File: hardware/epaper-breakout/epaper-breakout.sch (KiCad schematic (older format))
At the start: 88 parts, among them J1 XF2M-3315-1A, J2 C10418, J3 Conn_02x06_Counter_Clockwise, J4 ED060SC4, Q1 AO3401A, Q2 AO3401A, Q3 MMBT3904, Q4 MMBT3904, Q5 AO3401A, Q6 MMBT3904, U1 MCP1700-3302E_SOT23, U10 ED060SC7, U11 TP4056, U12 FS312F-G, U13 FS8205A, U2 LT1945, U3 LT1945, U4 CH340G, U5 ESP32-WROVER, U6 ED060XC5, U7 LM358, U8 74HC4094-normal, U9 MCP9700AT-ETT, Y1 Crystal_GND2

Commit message: remove battery protection, simplify
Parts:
- removed C13, C14: 10pF, Capacitor_SMD:C_0603_1608Metric, symbol Device:C
- removed C23: 0.1uF, Capacitor_SMD:C_0603_1608Metric, symbol Device:C
- removed R21: 100, Resistor_SMD:R_0805_2012Metric, symbol Device:R
- removed R22: 1k, Resistor_SMD:R_0805_2012Metric, symbol Device:R
- removed U12: FS312F-G, Package_TO_SOT_SMD:SOT-23-6, symbol epd_breakout:FS312F-G
- removed U13: FS8205A, Package_SO:TSSOP-8_4.4x3mm_P0.65mm, symbol fs8205a:FS8205A
- removed U4: CH340G, Package_SO:SOIC-16_3.9x9.9mm_P1.27mm, symbol Interface_USB:CH340G
- removed Y1: Crystal_GND2, Crystal:Crystal_SMD_3225-4Pin_3.2x2.5mm_HandSoldering, symbol Device:Crystal_GND2
- added U12: CH340C, Package_SO:SOIC-16_3.9x9.9mm_P1.27mm, symbol Interface_USB:CH340C
- added U4: XC6206PxxxMR, Package_TO_SOT_SMD:SOT-23, symbol Regulator_Linear:XC6206PxxxMR
- C22: LCSC C1588 -> C14663
- D7: LCSC (none) -> C8598
- L1, L2, L3, L4: LCSC C326331 -> C206321
- Q1: LCSC (none) -> C15127
- R2: LCSC (none) -> C17407
- R3, R8: LCSC (none) -> C17513
- R9: value 2k -> 6.8k; LCSC (none) -> C17772
- gave numbers to parts that had none: 1
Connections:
- net labels added: +3.3_Serial, VIN
- net labels removed: 5V
- wire segments 533 -> 480
- no-connect marks 29 -> 28

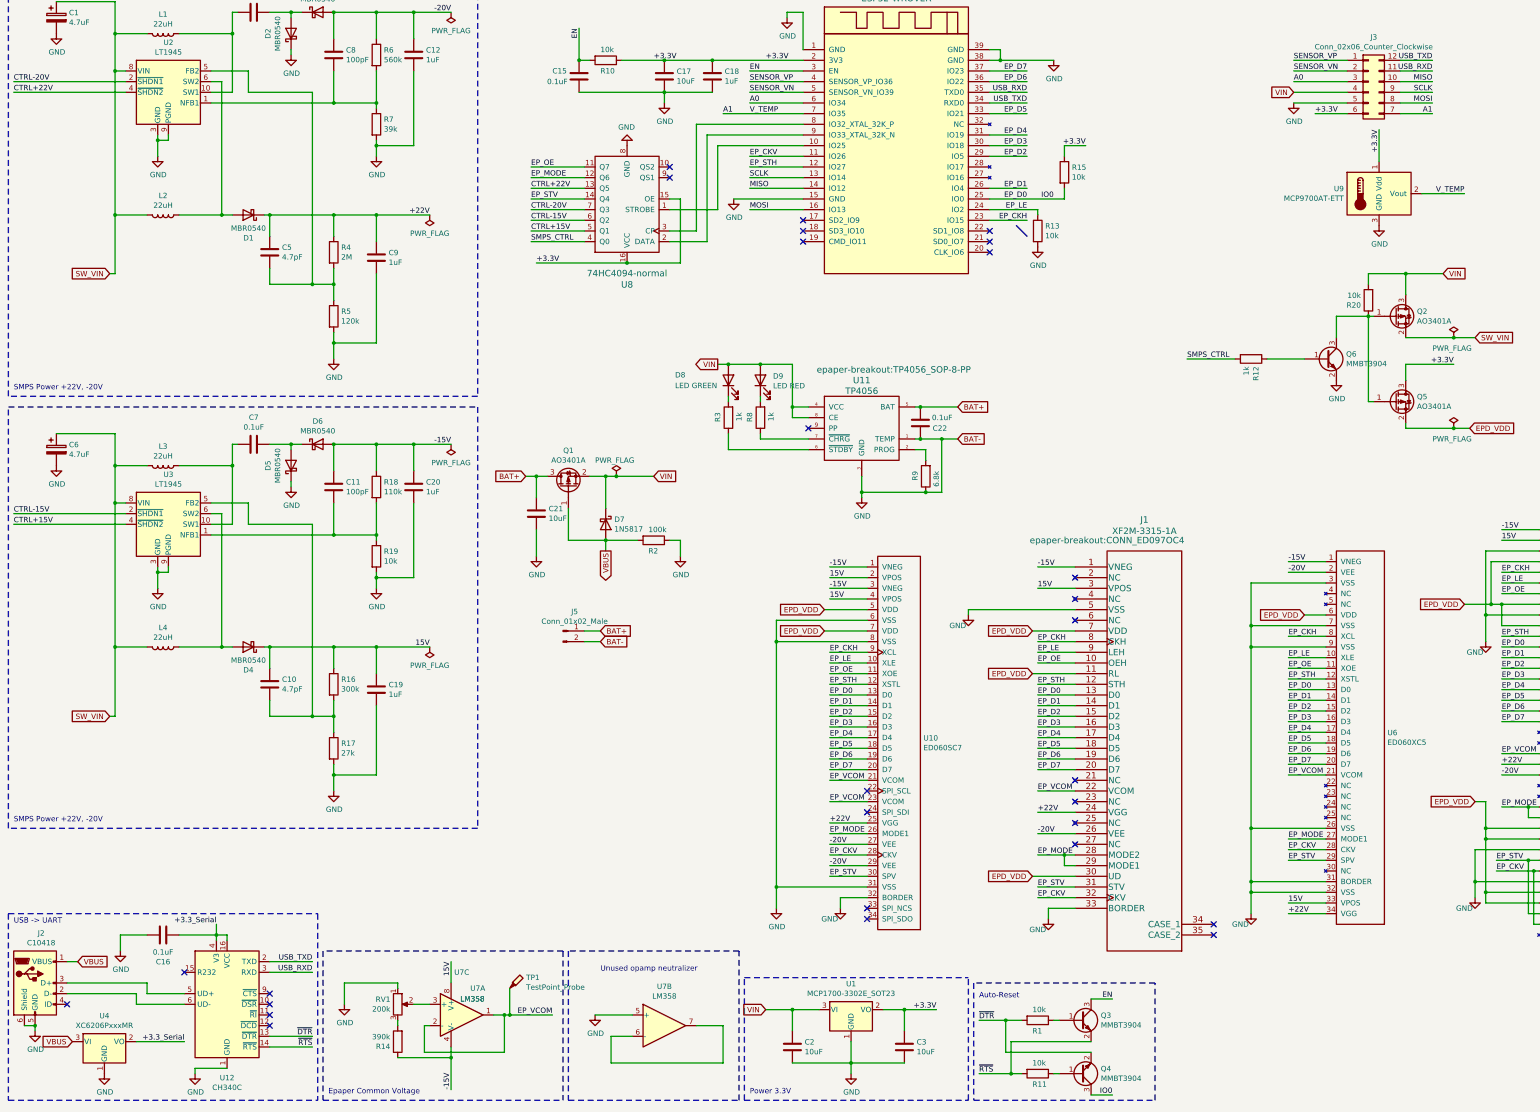
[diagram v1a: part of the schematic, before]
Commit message: add battery voltage sensing, routing
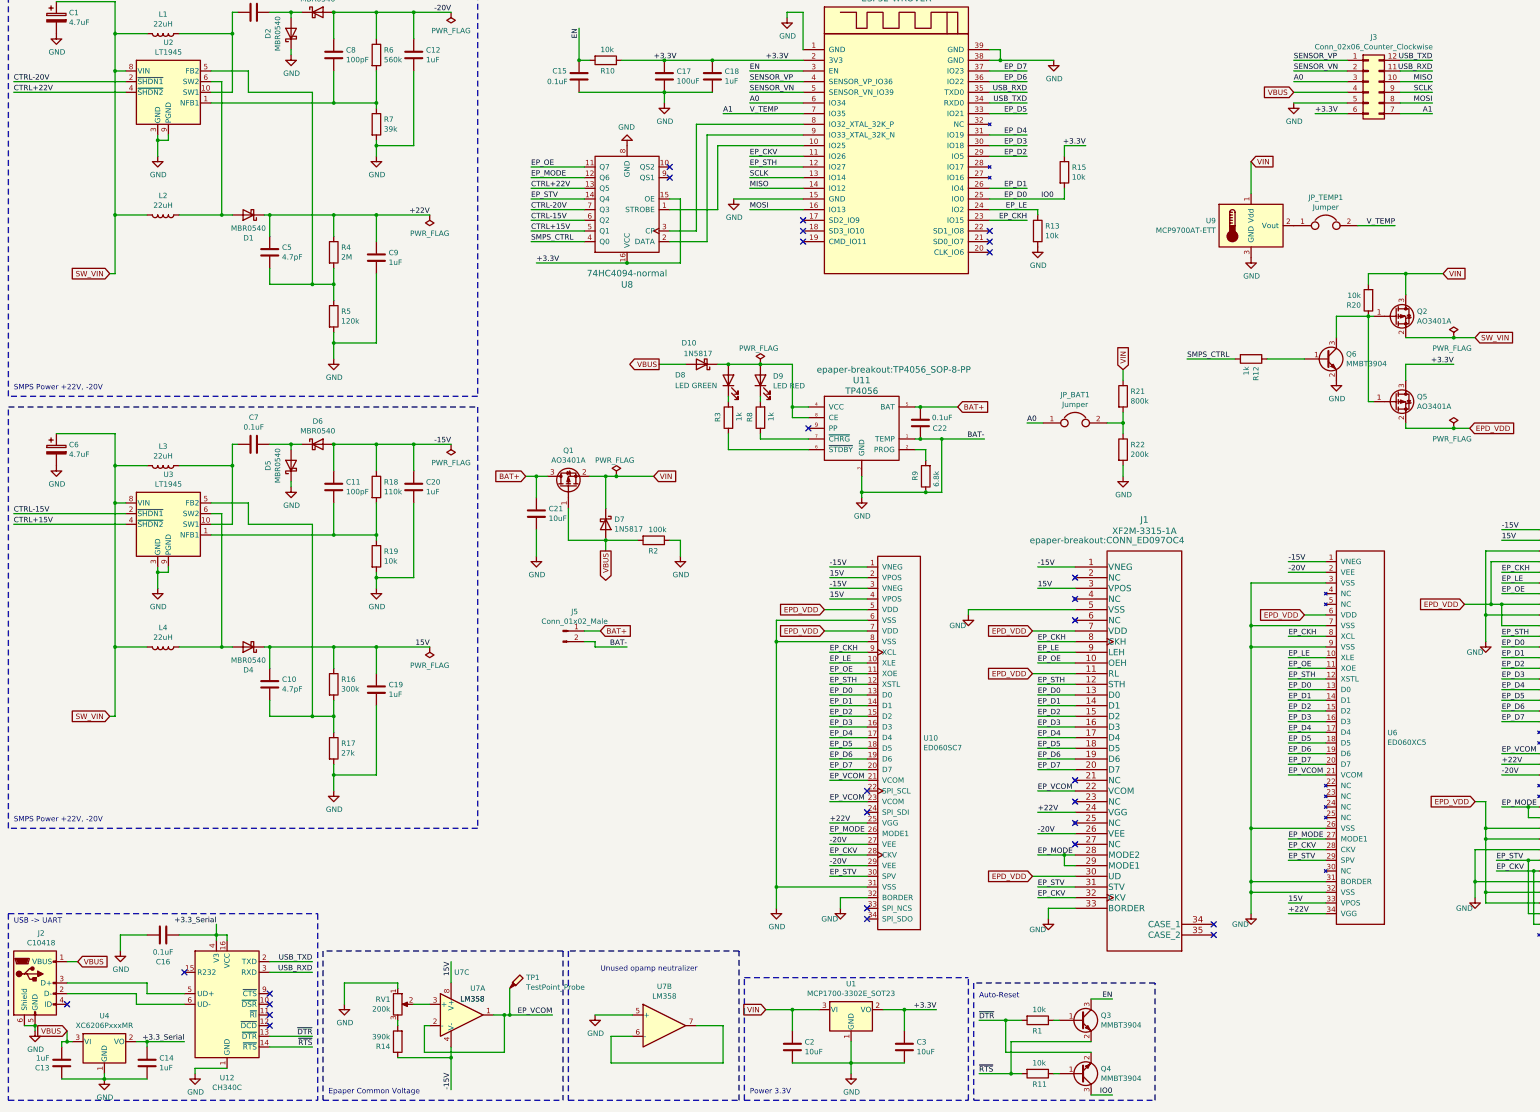
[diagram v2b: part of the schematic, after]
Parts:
- added C13, C14: 1uF, Capacitor_SMD:C_0603_1608Metric, symbol Device:C
- added D10: 1N5817, Diode_SMD:D_SOD-123, symbol Diode:1N5817
- added JP_BAT1, JP_TEMP1: Jumper, Jumper:SolderJumper-2_P1.3mm_Bridged2Bar_RoundedPad1.0x1.5mm, symbol Device:Jumper
- added R21: 800k, Resistor_SMD:R_0805_2012Metric, symbol Device:R
- added R22: 200k, Resistor_SMD:R_0805_2012Metric, symbol Device:R
- C17: value 10uF -> 100uF; footprint Capacitor_SMD:C_0603_1608Metric -> Capacitor_Tantalum_SMD:CP_EIA-3528-15_AVX-H; LCSC C19702 -> C16133
- U5: LCSC C503591 -> C503591
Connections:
- net +3.3V: no longer U9.1 (Vdd)
- net +3.3_Serial: now also C14.2
- net A0: now also JP_BAT1.1
- net A1: now also JP_TEMP1.2; no longer U9.2 (Vout)
- net GND: now also C13.2, C14.1, R22.2
- net VBUS: now also J3.4 (Pin_4), C13.1, D10.2 (A)
- net VIN: now also U9.1 (Vdd), R21.1; no longer D8.2 (A), D9.2 (A), J3.4 (Pin_4), U11.4 (VCC), U11.8 (CE)
- new net: JP_TEMP1.1, U9.2 (Vout)
- new net: D10.1 (K), D8.2 (A), D9.2 (A), U11.4 (VCC), U11.8 (CE)
- new net: JP_BAT1.2, R21.2, R22.1
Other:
- moved on the sheet: U9
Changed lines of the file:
@@
 F 2 "esp32-wrover:ESP32-WROVER" H 9350 1750 60  0001 C CNN
 F 3 "" H 9350 1750 60  0001 C CNN
-F 4 "C503591" H 8900 2050 50  0001 C CNN "LCSC"
+F 4 " C503591" H 8900 2050 50  0001 C CNN "LCSC"
 	1    8900 2050
 	1    0    0    -1
@@
 P 6700 1550
 F 0 "C17" H 6815 1596 50  0000 L CNN
-F 1 "10uF" H 6815 1505 50  0000 L CNN
-F 2 "Capacitor_SMD:C_0603_1608Metric" H 6738 1400 50  0001 C CNN
+F 1 "100uF" H 6815 1505 50  0000 L CNN
+F 2 "Capacitor_Tantalum_SMD:CP_EIA-3528-15_AVX-H" H 6738 1400 50  0001 C CNN
 F 3 "~" H 6700 1550 50  0001 C CNN
-F 4 "C19702" H 6700 1550 50  0001 C CNN "LCSC"
+F 4 " C16133" H 6700 1550 50  0001 C CNN "LCSC"
 	1    6700 1550
 	1    0    0    -1
@@
 L Sensor_Temperature:MCP9700AT-ETT U9
 U 1 1 5EB1CA91
-P 13400 2650
-F 0 "U9" H 13070 2696 50  0000 R CNN
-F 1 "MCP9700AT-ETT" H 13070 2605 50  0000 R CNN
-F 2 "Package_TO_SOT_SMD:SOT-23" H 13400 2250 50  0001 C CNN
-F 3 "http://ww1.microchip.com/downloads/en/DeviceDoc/21942e.pdf" H 13250 2900 50  0001 C CNN
-F 4 "C127949" H 13400 2650 50  0001 C CNN "LCSC"
-	1    13400 2650
+P 12200 2950
+F 0 "U9" H 11870 2996 50  0000 R CNN
+F 1 "MCP9700AT-ETT" H 11870 2905 50  0000 R CNN
+F 2 "Package_TO_SOT_SMD:SOT-23" H 12200 2550 50  0001 C CNN
+F 3 "http://ww1.microchip.com/downloads/en/DeviceDoc/21942e.pdf" H 12050 3200 50  0001 C CNN
+F 4 "C127949" H 12200 2950 50  0001 C CNN "LCSC"
+	1    12200 2950
 	1    0    0    -1
 $EndComp
 Text Label 7500 1900 0    50   ~ 0
 V_TEMP
-Text Label 14200 2650 2    50   ~ 0
+Text Label 13550 2950 2    50   ~ 0
 V_TEMP
 Wire Wire Line
-	14200 2650 13800 2650
-Text Label 13400 2050 3    50   ~ 0
-+3.3V
-Wire Wire Line
-	13400 2350 13400 2050
+	12200 2650 12200 2350
 Wire Wire Line
 	5950 2800 5450 2800
@@
 L power:GND #PWR07
 U 1 1 5EB6AA6D
-P 13400 2950
-F 0 "#PWR07" H 13400 2700 50  0001 C CNN
-F 1 "GND" H 13405 2777 50  0000 C CNN
-F 2 "" H 13400 2950 50  0001 C CNN
-F 3 "" H 13400 2950 50  0001 C CNN
-	1    13400 2950
+P 12200 3250
+F 0 "#PWR07" H 12200 3000 50  0001 C CNN
+F 1 "GND" H 12205 3077 50  0000 C CNN
+F 2 "" H 12200 3250 50  0001 C CNN
+F 3 "" H 12200 3250 50  0001 C CNN
+	1    12200 3250
 	1    0    0    -1
 $EndComp
@@
 	-1   0    0    1
 $EndComp
-Text GLabel 7200 4250 0    50   Output ~ 0
-VIN
+Text GLabel 6650 4250 0    50   Output ~ 0
+VBUS
 $Comp
 L power:GND #PWR011
@@
 	9050 4650 9100 4650
 Connection ~ 9100 4650
-NoConn ~ 8050 4850
 Text GLabel 1200 9850 2    50   Input ~ 0
 VBUS
@@
 Text GLabel 6100 6750 2    50   Input ~ 0
 BAT+
-Text GLabel 6100 6850 2    50   Input ~ 0
-BAT-
 Wire Wire Line
 	5950 6750 6100 6750
-Wire Wire Line
-	6100 6850 5950 6850
 Text GLabel 12600 1700 0    50   Input ~ 0
-VIN
+VBUS
 Wire Wire Line
 	9100 4650 9450 4650
-Text GLabel 9450 4950 2    50   Input ~ 0
-BAT-
-Wire Wire Line
-	9450 4950 9300 4950
 Connection ~ 9300 4950
 Connection ~ 6250 5300
@@
 Wire Wire Line
 	1100 9850 1200 9850
-Text GLabel 1150 10600 0    50   Input ~ 0
+Text GLabel 1100 10500 0    50   Input ~ 0
 VBUS
 Text Label 2200 10600 2    50   ~ 0
 +3.3_Serial
 Wire Wire Line
-	2200 10600 1750 10600
+	2200 10600 1850 10600
 $Comp
 L power:GND #PWR0103
 U 1 1 65E1BBDE
-P 1450 10900
-F 0 "#PWR0103" H 1450 10650 50  0001 C CNN
-F 1 "GND" H 1455 10727 50  0000 C CNN
-F 2 "" H 1450 10900 50  0001 C CNN
-F 3 "" H 1450 10900 50  0001 C CNN
-	1    1450 10900
+P 1450 10950
+F 0 "#PWR0103" H 1450 10700 50  0001 C CNN
+F 1 "GND" H 1455 10777 50  0000 C CNN
+F 2 "" H 1450 10950 50  0001 C CNN
+F 3 "" H 1450 10950 50  0001 C CNN
+	1    1450 10950
 	1    0    0    -1
 $EndComp
@@
 	1    0    0    -1
 $EndComp
-Entry Bus Bus
-	10000 2950 10100 3050
+$Comp
+L Diode:1N5817 D10
+U 1 1 65EFCF6E
+P 7050 4250
+F 0 "D10" H 7100 4050 50  0000 L CNN
+F 1 "1N5817" H 6950 4150 50  0000 L CNN
+F 2 "Diode_SMD:D_SOD-123" H 7050 4075 50  0001 C CNN
+F 3 "http://www.vishay.com/docs/88525/1n5817.pdf" H 7050 4250 50  0001 C CNN
+F 4 " C8598" V 7050 4250 50  0001 C CNN "LCSC"
+	1    7050 4250
+	-1   0    0    1
+$EndComp
+Wire Wire Line
+	6900 4250 6650 4250
+$Comp
+L Device:C C14
+U 1 1 66065C0C
+P 1850 10800
+F 0 "C14" H 1735 10754 50  0000 R CNN
+F 1 "1uF" H 1735 10845 50  0000 R CNN
+F 2 "Capacitor_SMD:C_0603_1608Metric" H 1888 10650 50  0001 C CNN
+F 3 "~" H 1850 10800 50  0001 C CNN
+F 4 "C15849" H 1850 10800 50  0001 C CNN "LCSC"
+	1    1850 10800
+	-1   0    0    1
+$EndComp
+$Comp
+L Device:C C13
+U 1 1 660AD8EC
+P 1050 10800
+F 0 "C13" H 935 10754 50  0000 R CNN
+F 1 "1uF" H 935 10845 50  0000 R CNN
+F 2 "Capacitor_SMD:C_0603_1608Metric" H 1088 10650 50  0001 C CNN
+F 3 "~" H 1050 10800 50  0001 C CNN
+F 4 "C15849" H 1050 10800 50  0001 C CNN "LCSC"
+	1    1050 10800
+	1    0    0    -1
+$EndComp
+Wire Wire Line
+	1100 10500 1100 10600
+Wire Wire Line
+	1100 10600 1150 10600
+Wire Wire Line
+	1100 10600 1050 10600
+Wire Wire Line
+	1050 10600 1050 10650
+Connection ~ 1100 10600
+Wire Wire Line
+	1050 10950 1450 10950
+Wire Wire Line
+	1450 10950 1450 10900
+Connection ~ 1450 10950
+Wire Wire Line
+	1450 10950 1850 10950
+Wire Wire Line
+	1850 10650 1850 10600
+Connection ~ 1850 10600
+Wire Wire Line
+	1850 10600 1750 10600
+Text GLabel 12200 2350 2    50   Input ~ 0
+VIN
+$Comp
+L Device:Jumper JP_TEMP1
+U 1 1 66377595
+P 12900 2950
+F 0 "JP_TEMP1" H 12900 3214 50  0000 C CNN
+F 1 "Jumper" H 12900 3123 50  0000 C CNN
+F 2 "Jumper:SolderJumper-2_P1.3mm_Bridged2Bar_RoundedPad1.0x1.5mm" H 12900 2950 50  0001 C CNN
+F 3 "~" H 12900 2950 50  0001 C CNN
+	1    12900 2950
+	1    0    0    -1
+$EndComp
+Wire Wire Line
+	13200 2950 13550 2950
+Text Label 10100 4800 0    50   ~ 0
+A0
+$Comp
+L Device:Jumper JP_BAT1
+U 1 1 6640F176
+P 10550 4800
+F 0 "JP_BAT1" H 10550 5064 50  0000 C CNN
+F 1 "Jumper" H 10550 4973 50  0000 C CNN
+F 2 "Jumper:SolderJumper-2_P1.3mm_Bridged2Bar_RoundedPad1.0x1.5mm" H 10550 4800 50  0001 C CNN
+F 3 "~" H 10550 4800 50  0001 C CNN
+	1    10550 4800
+	1    0    0    -1
+$EndComp
+Wire Wire Line
+	10100 4800 10250 4800
+$Comp
+L Device:R R22
+U 1 1 6653BFFD
+P 11000 5050
+F 0 "R22" H 11070 5096 50  0000 L CNN
+F 1 "200k" H 11070 5005 50  0000 L CNN
+F 2 "Resistor_SMD:R_0805_2012Metric" V 10930 5050 50  0001 C CNN
+F 3 "~" H 11000 5050 50  0001 C CNN
+	1    11000 5050
+	1    0    0    -1
+$EndComp
+$Comp
+L Device:R R21
+U 1 1 66586D13
+P 11000 4550
+F 0 "R21" H 11070 4596 50  0000 L CNN
+F 1 "800k" H 11070 4505 50  0000 L CNN
+F 2 "Resistor_SMD:R_0805_2012Metric" V 10930 4550 50  0001 C CNN
+F 3 "~" H 11000 4550 50  0001 C CNN
+	1    11000 4550
+	1    0    0    -1
+$EndComp
+$Comp
+L power:GND #PWR0121
+U 1 1 666FDC76
+P 11000 5300
+F 0 "#PWR0121" H 11000 5050 50  0001 C CNN
+F 1 "GND" H 11005 5127 50  0000 C CNN
+F 2 "" H 11000 5300 50  0001 C CNN
+F 3 "" H 11000 5300 50  0001 C CNN
+	1    11000 5300
+	1    0    0    -1
+$EndComp
+Wire Wire Line
+	11000 4300 11000 4400
+Wire Wire Line
+	10850 4800 11000 4800
+Wire Wire Line
+	11000 4800 11000 4700
+Wire Wire Line
+	11000 4800 11000 4900
+Connection ~ 11000 4800
+Wire Wire Line
+	11000 5200 11000 5300
+Text Label 9700 4950 2    50   ~ 0
+BAT-
+Wire Wire Line
+	9300 4950 9700 4950
+Text Label 6350 6900 2    50   ~ 0
+BAT-
+Wire Wire Line
+	5950 6850 6050 6850
+Wire Wire Line
+	6050 6850 6050 6900
+Wire Wire Line
+	6050 6900 6350 6900
+$Comp
+L power:PWR_FLAG #FLG0103
+U 1 1 66A7D201
+P 7600 4250
+F 0 "#FLG0103" H 7600 4325 50  0001 C CNN
+F 1 "PWR_FLAG" H 7400 4400 50  0000 L CNN
+F 2 "" H 7600 4250 50  0001 C CNN
+F 3 "~" H 7600 4250 50  0001 C CNN
+	1    7600 4250
+	1    0    0    -1
+$EndComp
+Text GLabel 11000 4300 1    50   Input ~ 0
+VIN
+NoConn ~ 8050 4850
 $EndSCHEMATC

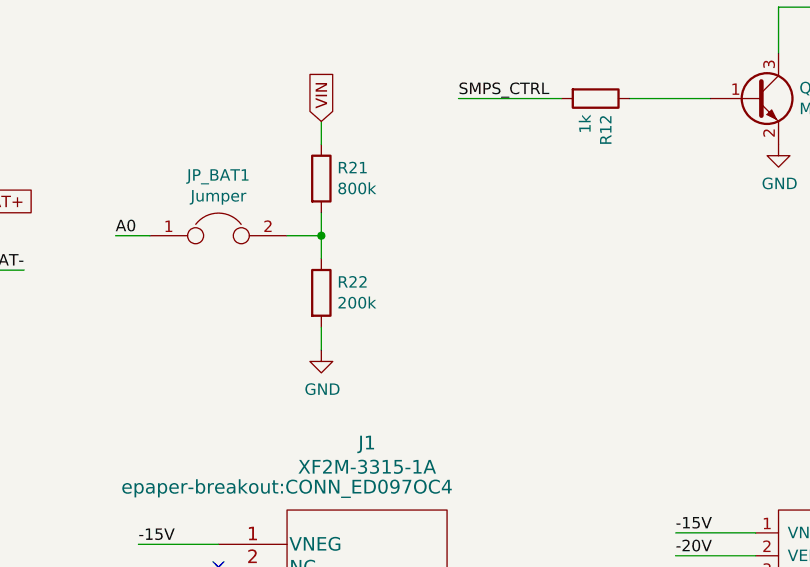
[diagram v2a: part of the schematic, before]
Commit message: add decoupling cap to battery voltage sensor
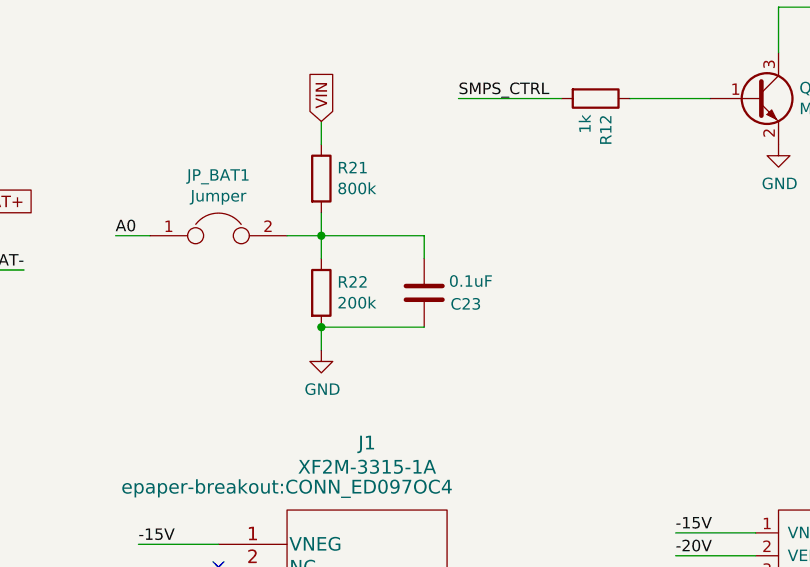
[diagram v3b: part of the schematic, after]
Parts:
- added C23: 0.1uF, Capacitor_SMD:C_0603_1608Metric, symbol Device:C
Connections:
- net GND: now also C23.1
- net at JP_BAT1.2, R21.2, R22.1: now also C23.2
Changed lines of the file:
@@
 VIN
 NoConn ~ 8050 4850
+$Comp
+L Device:C C23
+U 1 1 5FF94231
+P 11450 5050
+F 0 "C23" H 11700 5100 50  0000 R CNN
+F 1 "0.1uF" H 11750 5000 50  0000 R CNN
+F 2 "Capacitor_SMD:C_0603_1608Metric" H 11488 4900 50  0001 C CNN
+F 3 "~" H 11450 5050 50  0001 C CNN
+F 4 "C14663" V 11450 5050 50  0001 C CNN "LCSC"
+	1    11450 5050
+	1    0    0    1
+$EndComp
+Wire Wire Line
+	11000 4800 11450 4800
+Wire Wire Line
+	11450 4800 11450 4900
+Wire Wire Line
+	11450 5200 11000 5200
+Connection ~ 11000 5200
 $EndSCHEMATC
